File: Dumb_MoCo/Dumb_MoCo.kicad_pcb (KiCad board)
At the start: 2 copper layers, 33.3 x 52.8 mm, 17 parts, among them U1 VNH5050A-E

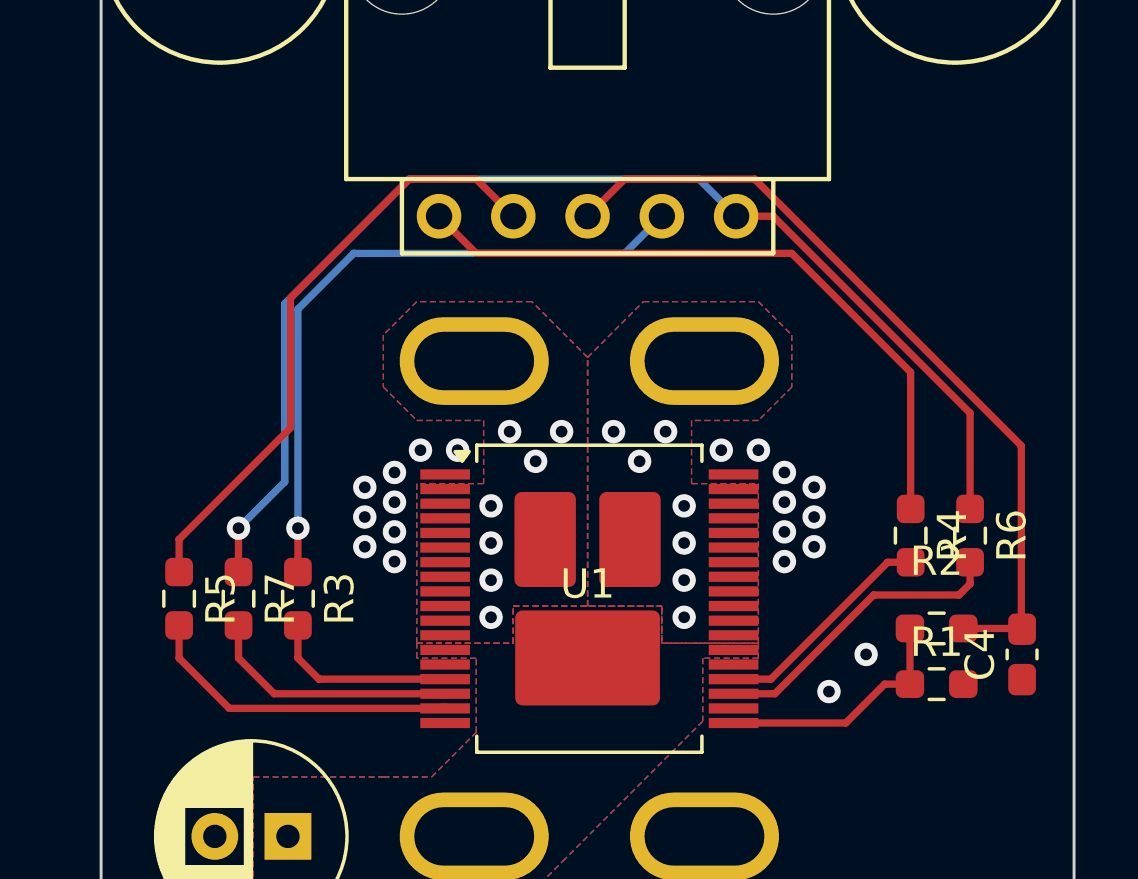
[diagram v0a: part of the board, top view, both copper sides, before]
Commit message: Moved up vias, connected pads with fat trace
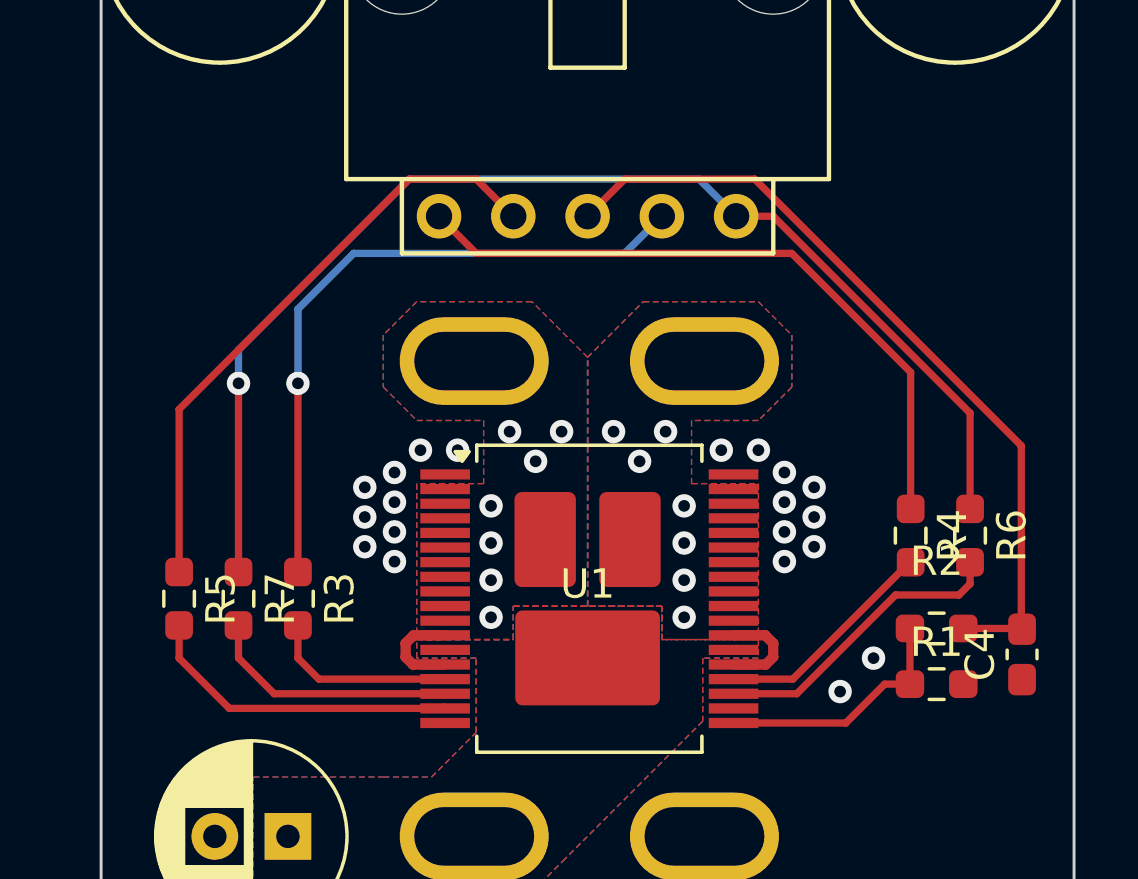
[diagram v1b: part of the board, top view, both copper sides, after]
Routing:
- net Net-(Conn1B-V+Log): track 0.00 -> 3.40 mm
- net Net-(Conn1A-GND): track 0.00 -> 3.39 mm
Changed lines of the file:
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@@
 	)
 	(setup
+		(stackup
+			(layer "F.SilkS"
+				(type "Top Silk Screen")
+			)
+			(layer "F.Paste"
+				(type "Top Solder Paste")
+			)
+			(layer "F.Mask"
+				(type "Top Solder Mask")
+				(thickness 0.01)
+			)
+			(layer "F.Cu"
+				(type "copper")
+				(thickness 0.035)
+			)
+			(layer "dielectric 1"
+				(type "core")
+				(thickness 1.51)
+				(material "FR4")
+				(epsilon_r 4.5)
+				(loss_tangent 0.02)
+			)
+			(layer "B.Cu"
+				(type "copper")
+				(thickness 0.035)
+			)
+			(layer "B.Mask"
+				(type "Bottom Solder Mask")
+				(thickness 0.01)
+			)
+			(layer "B.Paste"
+				(type "Bottom Solder Paste")
+			)
+			(layer "B.SilkS"
+				(type "Bottom Silk Screen")
+			)
+			(copper_finish "None")
+			(dielectric_constraints no)
+		)
 		(pad_to_mask_clearance 0)
 		(allow_soldermask_bridges_in_footprints no)
@@
 	)
 	(via
-		(at 198.755 66.675)
+		(at 199.136 66.675)
 		(size 0.8)
 		(drill 0.4)
@@
 	)
 	(via
-		(at 200.025 65.405)
+		(at 200.279 65.532)
 		(size 0.8)
 		(drill 0.4)
@@
 		(net 3)
 	)
+	(segment
+		(start 195.4925 65.75)
+		(end 196.5925 65.75)
+		(width 0.3556)
+		(layer "F.Cu")
+		(net 4)
+	)
+	(segment
+		(start 196.576 64.75)
+		(end 195.4925 64.75)
+		(width 0.3556)
+		(layer "F.Cu")
+		(net 4)
+	)
+	(segment
+		(start 196.85 65.4925)
+		(end 196.85 65.024)
+		(width 0.3556)
+		(layer "F.Cu")
+		(net 4)
+	)
+	(segment
+		(start 196.5925 65.75)
+		(end 196.85 65.4925)
+		(width 0.3556)
+		(layer "F.Cu")
+		(net 4)
+	)
+	(segment
+		(start 196.85 65.024)
+		(end 196.576 64.75)
+		(width 0.3556)
+		(layer "F.Cu")
+		(net 4)
+	)
 	(via
 		(at 192.278 58.801)
@@
 		(net 4)
 	)
+	(segment
+		(start 184.551 64.75)
+		(end 185.6275 64.75)
+		(width 0.3556)
+		(layer "F.Cu")
+		(net 5)
+	)
+	(segment
+		(start 184.277 65.024)
+		(end 184.551 64.75)
+		(width 0.3556)
+		(layer "F.Cu")
+		(net 5)
+	)
+	(segment
+		(start 185.6275 65.75)
+		(end 184.5275 65.75)
+		(width 0.3556)
+		(layer "F.Cu")
+		(net 5)
+	)
+	(segment
+		(start 184.277 65.4995)
+		(end 184.277 65.024)
+		(width 0.3556)
+		(layer "F.Cu")
+		(net 5)
+	)
+	(segment
+		(start 184.5275 65.75)
+		(end 184.277 65.4995)
+		(width 0.3556)
+		(layer "F.Cu")
+		(net 5)
+	)
 	(via
 		(at 189.611 57.785)
@@
 	(segment
 		(start 180.594 62.5875)
-		(end 180.594 61.087)
+		(end 180.594 56.134)
 		(width 0.25)
 		(layer "F.Cu")
@@
 	)
 	(via
-		(at 180.594 61.087)
+		(at 180.594 56.134)
 		(size 0.8)
 		(drill 0.4)
@@
 	)
 	(segment
-		(start 191.77 51.689)
-		(end 193.04 50.419)
+		(start 182.500396 51.689)
+		(end 191.77 51.689)
 		(width 0.25)
 		(layer "B.Cu")
@@
 	)
 	(segment
-		(start 180.594 61.087)
-		(end 180.594 53.595396)
+		(start 180.594 53.595396)
+		(end 182.500396 51.689)
 		(width 0.25)
 		(layer "B.Cu")
@@
 	)
 	(segment
-		(start 180.594 53.595396)
-		(end 182.500396 51.689)
+		(start 191.77 51.689)
+		(end 193.04 50.419)
 		(width 0.25)
 		(layer "B.Cu")
@@
 	)
 	(segment
-		(start 182.500396 51.689)
-		(end 191.77 51.689)
+		(start 180.594 56.134)
+		(end 180.594 53.595396)
 		(width 0.25)
 		(layer "B.Cu")
@@
 	)
 	(segment
-		(start 200.7635 62.2535)
-		(end 196.767 66.25)
+		(start 197.518299 66.25)
+		(end 195.4925 66.25)
 		(width 0.25)
 		(layer "F.Cu")
@@
 	(segment
 		(start 201.549 62.2535)
-		(end 200.7635 62.2535)
+		(end 201.514799 62.2535)
 		(width 0.25)
 		(layer "F.Cu")
@@
 	)
 	(segment
-		(start 196.767 66.25)
-		(end 195.4925 66.25)
+		(start 201.514799 62.2535)
+		(end 197.518299 66.25)
 		(width 0.25)
 		(layer "F.Cu")
@@
 	)
 	(segment
-		(start 176.53 62.5875)
-		(end 176.53 61.468)
+		(start 186.69 49.149)
+		(end 187.96 50.419)
 		(width 0.25)
 		(layer "F.Cu")
@@
 	)
 	(segment
-		(start 180.34 53.213)
+		(start 176.53 57.023)
 		(end 184.404 49.149)
 		(width 0.25)
@@
 	)
 	(segment
-		(start 180.34 57.658)
-		(end 180.34 53.213)
-		(width 0.25)
-		(layer "F.Cu")
-		(net 12)
-	)
-	(segment
-		(start 176.53 61.468)
-		(end 180.34 57.658)
-		(width 0.25)
-		(layer "F.Cu")
-		(net 12)
-	)
-	(segment
-		(start 186.69 49.149)
-		(end 187.96 50.419)
+		(start 176.53 62.5875)
+		(end 176.53 57.023)
 		(width 0.25)
 		(layer "F.Cu")
@@
 	)
 	(segment
-		(start 203.581 57.151396)
-		(end 203.581 60.4285)
+		(start 178.562 62.5875)
+		(end 178.562 56.134)
 		(width 0.25)
 		(layer "F.Cu")
@@
 	)
 	(segment
-		(start 178.562 62.5875)
-		(end 178.562 61.087)
+		(start 203.581 57.151396)
+		(end 203.581 60.4285)
 		(width 0.25)
 		(layer "F.Cu")
@@
 	)
 	(via
-		(at 178.562 61.087)
+		(at 178.562 56.134)
 		(size 0.8)
 		(drill 0.4)
@@
 	)
 	(segment
-		(start 178.562 61.087)
-		(end 180.144 59.505)
+		(start 178.562 54.991)
+		(end 184.404 49.149)
 		(width 0.25)
 		(layer "B.Cu")
@@
 	)
 	(segment
-		(start 180.144 59.505)
-		(end 180.144 53.409)
-		(width 0.25)
-		(layer "B.Cu")
-		(net 13)
-	)
-	(segment
-		(start 180.144 53.409)
-		(end 184.404 49.149)
+		(start 178.562 56.134)
+		(end 178.562 54.991)
 		(width 0.25)
 		(layer "B.Cu")
@@
 	)
 	(segment
-		(start 203.2 63.373)
-		(end 200.280396 63.373)
+		(start 201.031695 63.373)
+		(end 197.654695 66.75)
 		(width 0.25)
 		(layer "F.Cu")
@@
 	)
 	(segment
-		(start 200.280396 63.373)
-		(end 196.903396 66.75)
+		(start 203.581 62.992)
+		(end 203.2 63.373)
 		(width 0.25)
 		(layer "F.Cu")
@@
 	)
 	(segment
-		(start 203.581 62.992)
-		(end 203.2 63.373)
+		(start 197.654695 66.75)
+		(end 195.4925 66.75)
 		(width 0.25)
 		(layer "F.Cu")
@@
 	)
 	(segment
-		(start 196.903396 66.75)
-		(end 195.4925 66.75)
+		(start 203.2 63.373)
+		(end 201.031695 63.373)
 		(width 0.25)
 		(layer "F.Cu")
@@
 		(polygon
 			(pts
-				(xy 184.658 65.024) (xy 187.96 65.024) (xy 187.96 63.754) (xy 190.5 63.754) (xy 190.5 55.245) (xy 188.595 53.34)
+				(xy 184.658 64.897) (xy 187.96 64.897) (xy 187.96 63.754) (xy 190.5 63.754) (xy 190.5 55.245) (xy 188.595 53.34)
 				(xy 184.658 53.34) (xy 183.515 54.483) (xy 183.515 56.261) (xy 184.658 57.404) (xy 186.944 57.404)
 				(xy 186.944 59.563) (xy 184.658 59.563)
@@
 		(polygon
 			(pts
-				(xy 196.342 65.024) (xy 193.04 65.024) (xy 193.04 63.754) (xy 190.5 63.754) (xy 190.5 55.245) (xy 192.405 53.34)
+				(xy 196.342 64.897) (xy 193.04 64.897) (xy 193.04 63.754) (xy 190.5 63.754) (xy 190.5 55.245) (xy 192.405 53.34)
 				(xy 196.342 53.34) (xy 197.485 54.483) (xy 197.485 56.261) (xy 196.342 57.404) (xy 194.056 57.404)
 				(xy 194.056 59.563) (xy 196.342 59.563)
@@
 		(polygon
 			(pts
-				(xy 187.96 63.754) (xy 193.04 63.754) (xy 193.04 65.024) (xy 196.342 65.024) (xy 196.342 65.532)
+				(xy 187.96 63.754) (xy 193.04 63.754) (xy 193.04 64.897) (xy 196.342 64.897) (xy 196.342 65.532)
 				(xy 194.437 65.532) (xy 194.437 67.691) (xy 189.738 72.39) (xy 188.468 73.66) (xy 183.515 73.66)
 				(xy 182.88 73.66) (xy 179.07 73.66) (xy 179.07 69.596) (xy 183.515 69.596) (xy 185.166 69.596) (xy 186.69 68.072)
-				(xy 186.69 65.532) (xy 184.658 65.532) (xy 184.658 65.024) (xy 187.96 65.024)
+				(xy 186.69 65.532) (xy 184.658 65.532) (xy 184.658 64.897) (xy 187.96 64.897)
 			)
 		)

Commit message: Added silkscreens
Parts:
- added G***: LOGO, MRDT_Silkscreens:0_MRDT_Logo_10mm, F.Cu at (192.3, 83.3)
- added G***: LOGO, Signatures:WillGroveSignatureMedium, F.Cu at (176.9, 52.2)
- added G***: LOGO, Signatures:ChamberUlt, B.Cu at (190.5, 63.5)
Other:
- board text added: "12V"
- board text added: "3V3"
- board text added: "A"
- board text added: "B"
- board text added: "CS"
- board text added: "Dumb MoCo, Rev1 Mars Rover Design Team Missouri S&T, 2025 Will Grove"
- board text added: "GND"
- board text added: "M+"
- board text added: "M-"
- board text added: "PWM"
